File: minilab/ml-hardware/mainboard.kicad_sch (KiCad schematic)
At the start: 9 parts

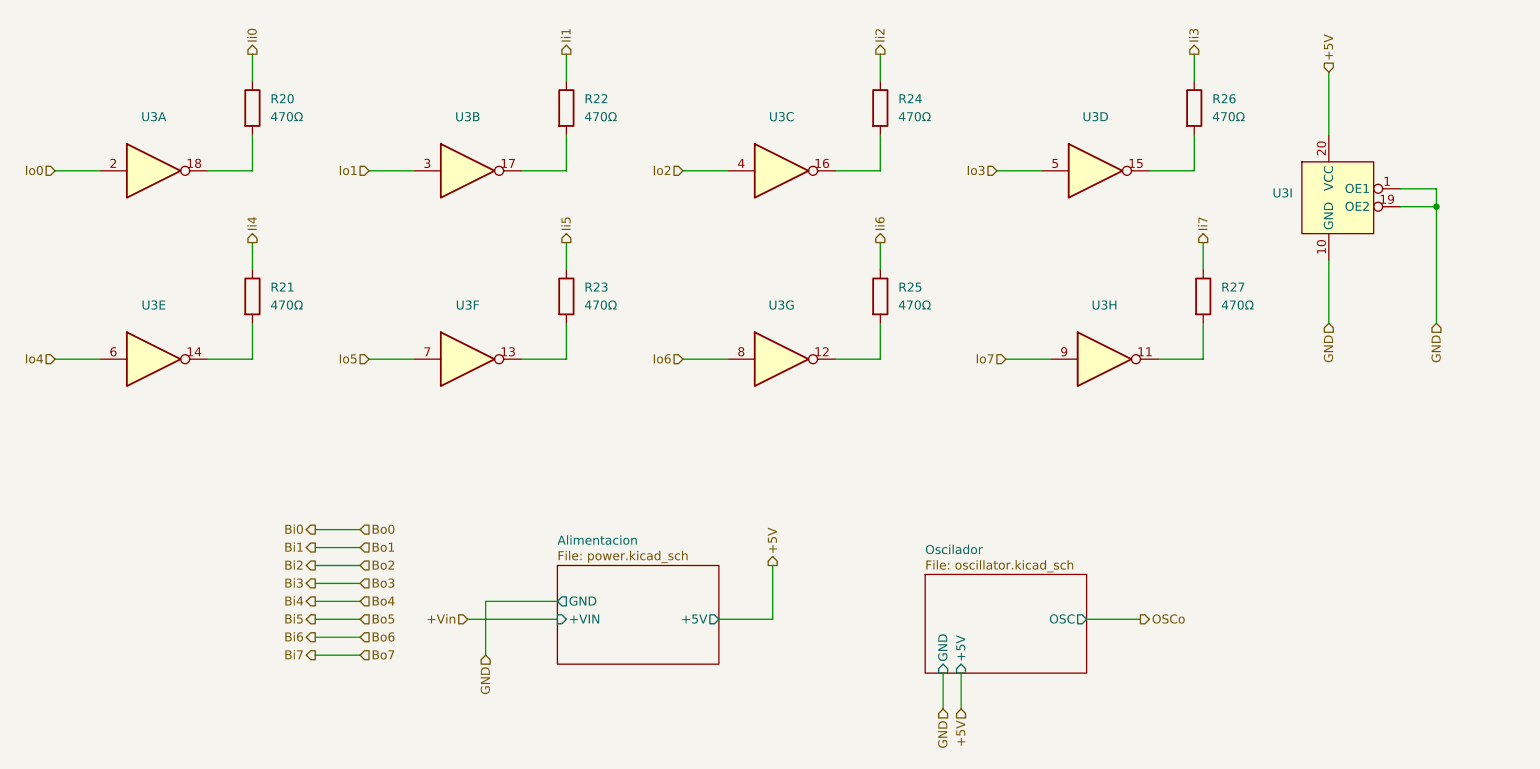
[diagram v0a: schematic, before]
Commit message: Dev minilab (#1)
* minilab: Add PCB (wip)

* minilab: Added fp and sym lib tables

* minilab: cambia jerarquia y agrega pcb

* minilab: Agrega 2da opc conectores y modelos 3d
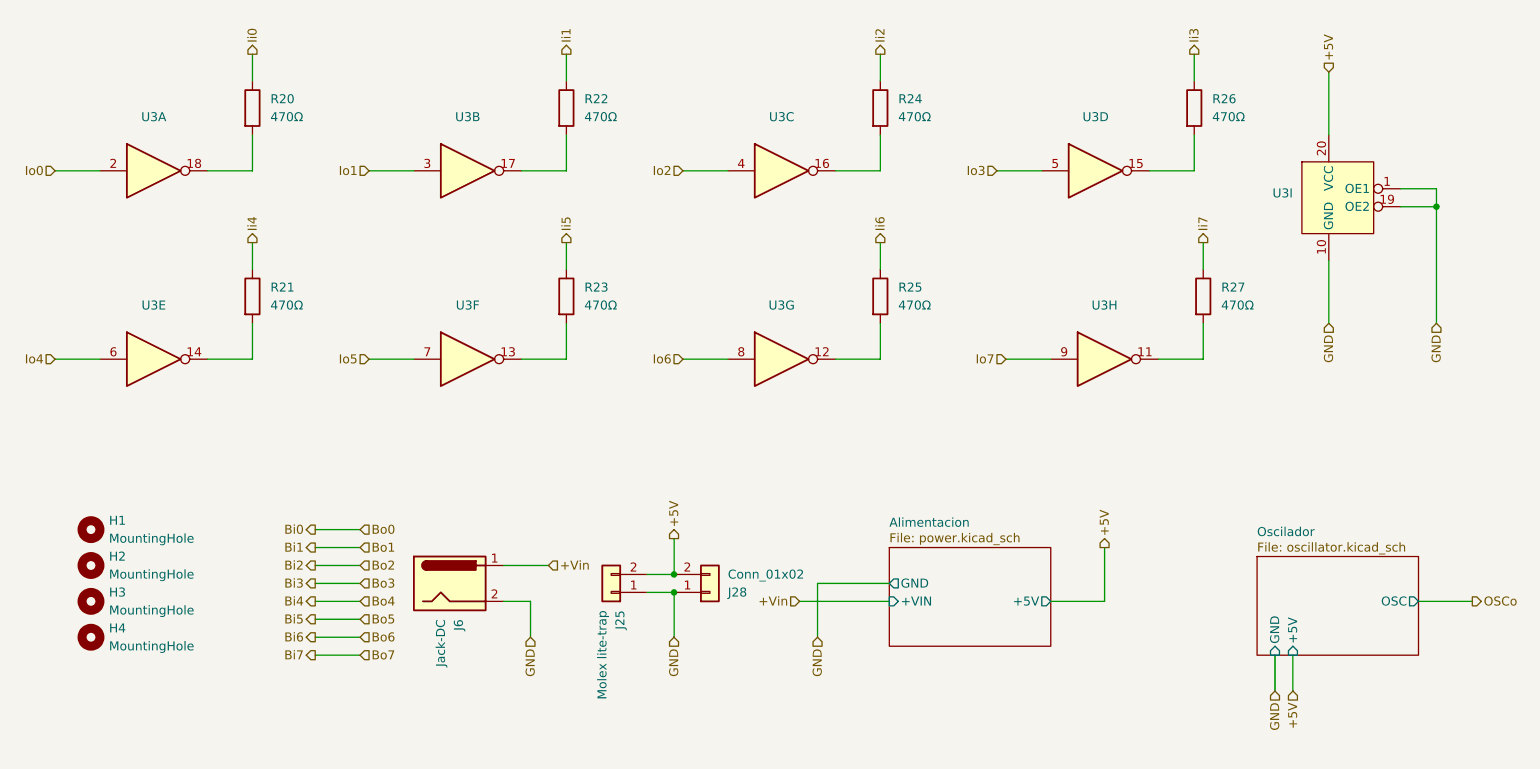
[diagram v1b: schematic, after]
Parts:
- added H1, H2, H3, H4: MountingHole, MountingHole:MountingHole_3.2mm_M3, symbol Mechanical:MountingHole
- added J25: Molex lite-trap, Extras:104238-0210, symbol Connector_Generic:Conn_01x02
- added J28: Conn_01x02, Connector_PinSocket_2.54mm:PinSocket_1x02_P2.54mm_Horizontal, symbol Connector_Generic:Conn_01x02
- added J6: Jack-DC, Connector_BarrelJack:BarrelJack_Horizontal, symbol Connector:Jack-DC
- R20, R27: footprint Resistor_THT:R_Axial_DIN0204_L3.6mm_D1.6mm_P5.08mm_Horizontal -> Resistor_THT:R_Axial_DIN0204_L3.6mm_D1.6mm_P7.62mm_Horizontal
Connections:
- net +5V: now also J25.2 (Pin_2), J28.2 (Pin_2)
- net +Vin: now also J6.1
- net GND: now also J25.1 (Pin_1), J28.1 (Pin_1), J6.2
